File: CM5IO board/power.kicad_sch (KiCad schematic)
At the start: 0 parts

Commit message: Duplicated additional USB-C in sch.
How to change pin label on CM5?
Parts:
- added C31, C35, C37: 10uF, Capacitor_SMD:C_0402_1005Metric, symbol Device:C_Small
- added C32: 10uF, Capacitor_SMD:C_0603_1608Metric, symbol Device:C_Small
- added C33: 1uF, Capacitor_SMD:C_0402_1005Metric, symbol Device:C_Small
- added C34: 22uF, Capacitor_SMD:C_0603_1608Metric, symbol Device:C_Small
- added C36: 4.7uF, Capacitor_SMD:C_0402_1005Metric, symbol Device:C_Small
- added C38: 0.1uF, Capacitor_SMD:C_0402_1005Metric, symbol Device:C_Small
- added L3: 1uH, Inductor_SMD:L_0805_2012Metric, symbol Device:L
- added R27, R30: 10k, Resistor_SMD:R_0402_1005Metric, symbol Device:R_Small
- added R28: 14k, Resistor_SMD:R_0402_1005Metric, symbol Device:R_Small
- added R29: 56k, Resistor_SMD:R_0402_1005Metric, symbol Device:R_Small
- added TP11, TP12, TP8 (x2): TestPoint, TestPoint:TestPoint_Pad_D1.5mm, symbol Connector:TestPoint
- added U3: LM66200DRLR, iclr:SOTFL50P160X60-8N, symbol iclr:LM66200DRLR
- added U4: MAX77827AEFD+T, iclr:CONV_MAX77827AEFD+T, symbol iclr:MAX77827AEFD+T
- added U5: SC4215ASTRT, iclr:SOIC127P599X175-9N, symbol iclr:SC4215ASTRT
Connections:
- new net: R27.2, U3.8 (ST)
- new net +3V3: C37.2, C38.2, R29.1, TP12.1, U5.6 (VOUT)
- new net BBIN: C31.1, C32.1, TP8.1, U3.2 (VOUT_1), U3.7 (VOUT_2), U4.3 (EN), U4.6 (IN)
- new net BBOUT: C34.1, C35.1, C36.1, TP8.1, U4.11 (OUT), U4.13 (OUTS), U5.2 (EN), U5.3 (VIN)
- new net BIAS: C33.1, U4.5 (BIAS)
- new net FBIn: R29.2, R30.1, U5.7 (ADJ)
- new net GND: C31.2, C32.2, C33.2, C34.2, C35.2, C36.2, C37.1, C38.1, R28.2, R30.2, U3.1 (GND_1), U3.4 (~{ON}), U3.5 (GND_2), U4.4 (AGND), U4.9 (PGND), U5.8 (GND), U5.9 (GND)
- new net LX1: L3.1, U4.8 (LX1)
- new net LX2: L3.2, U4.10 (LX2)
- new net RBUS_uC_V: TP11.1, U3.6 (VIN2)
- new net SEL: R28.1, U4.1 (SEL)
- new net VBUS: R27.1, U3.3 (VIN1)
- no-connect marks 0 -> 4
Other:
- note added: "Be extra careful in leaving this connected at a single point"
- note added: "Place close together. Bridge to bypass buck-boost"

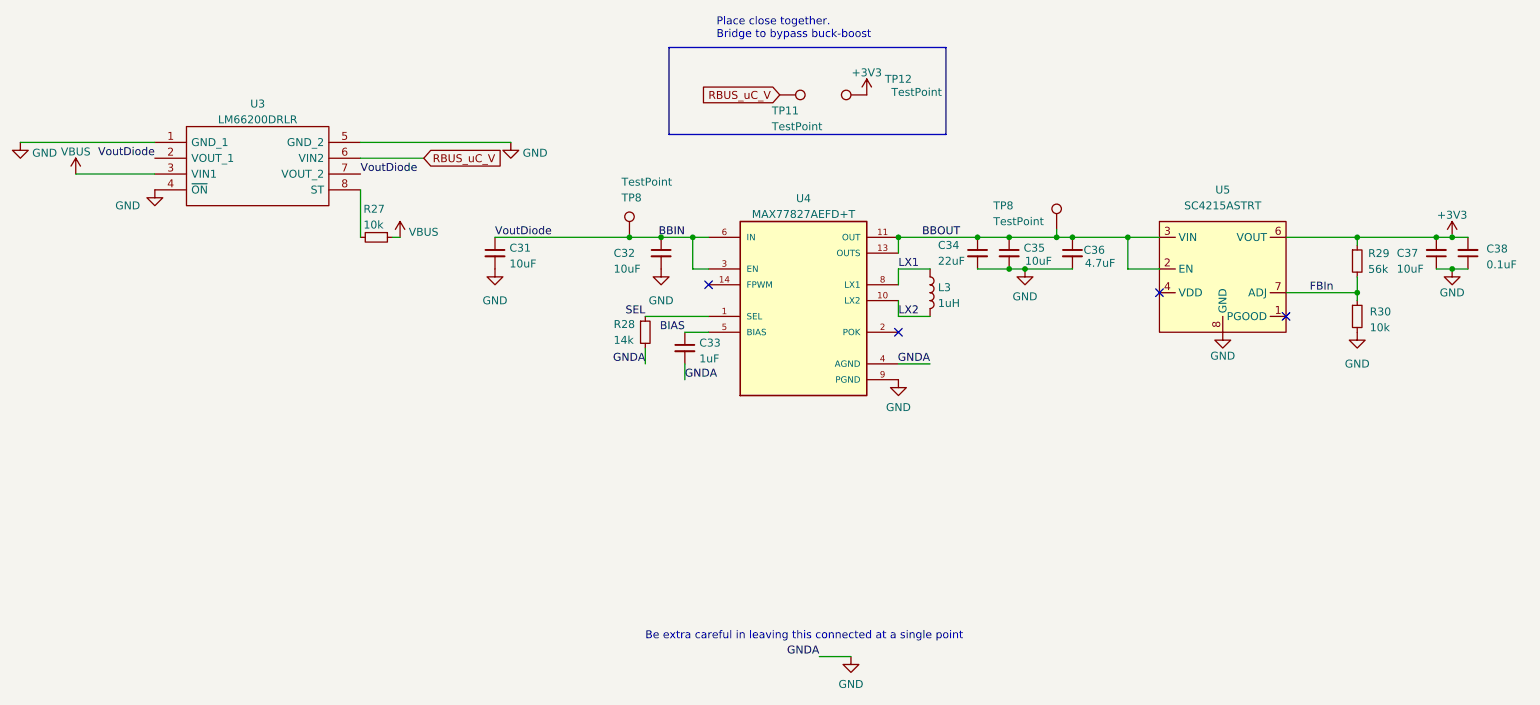
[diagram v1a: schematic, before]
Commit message: Moved Ricardo to hierarchical sheet in main sch.
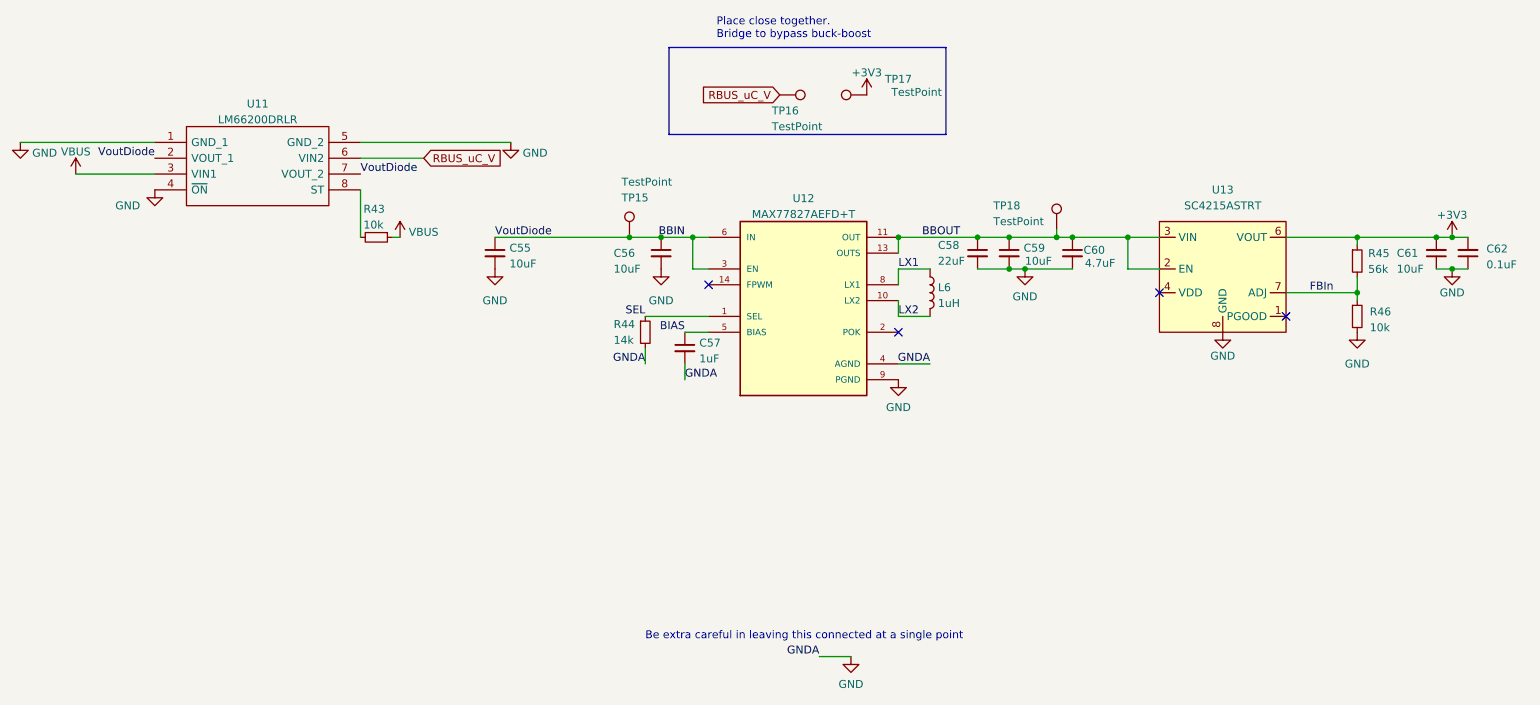
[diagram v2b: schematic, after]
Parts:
- renumbered C31 to C55, C32 to C56, C33 to C57, C34 to C58, C35 to C59, C36 to C60, C37 to C61, C38 to C62, L3 to L6, R27 to R43, R28 to R44, R29 to R45, R30 to R46, TP8 to TP15, TP11 to TP16, TP12 to TP17, TP8 to TP18, U3 to U11, U4 to U12, U5 to U13
